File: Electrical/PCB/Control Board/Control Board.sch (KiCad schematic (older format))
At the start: 89 parts, among them J1 ED2627-ND, J10 6posheader, J11 S7038-ND, J12 ED2989-ND-USB, J13 ED1501-ND, J14 ED2989-ND-USB, J15 ED2580-ND, J16 ED2580-ND, J17 ED2744-ND, J18 ED2744-ND, J19 ED2744-ND, J2 ED2627-ND, J20 ED2744-ND, J21 ED2744-ND, J22 ED2744-ND, J23 ED2744-ND, J24 ED2744-ND, J25 ED2744-ND, J26 ED2744-ND, J3 ED2627-ND, J4 ED2627-ND, J5 ED2627-ND, J6 S9175-ND, J7 S9175-ND, J8 6posheader, J9 S7038-ND, M1 Mounting_Holes, T1 test_point, T10 test_point, T11 test_point, T12 test_point, T13 test_point, T14 test_point, T15 test_point, T16 test_point, T17 test_point, T18 test_point, T19 test_point, T2 test_point, T20 test_point, T21 test_point, T3 test_point, T4 test_point, T5 test_point, T6 test_point, T7 test_point, T8 test_point, T9 test_point, U1 LM358-N, U2 LM358-N, y1 rover_silkscreen

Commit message: Initial PCB corrections
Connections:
- wire segments 460 -> 462
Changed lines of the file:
@@
 EESchema Schematic File Version 4
-LIBS:Control Board-cache
-EELAYER 26 0
+EELAYER 30 0
 EELAYER END
 $Descr A3 16535 11693
@@
 	-1   0    0    -1
 $EndComp
-Text Label 6150 7300 0    50   ~ 0
-+BATT
 $Comp
 L Control-Board-rescue:#6THRU-HOLE-JPL_Robotics_Lib-Monolithic-Board-rescue MH1
@@
 	5950 6100 6150 6100
 Wire Wire Line
-	5900 7300 6150 7300
-Wire Wire Line
-	14200 8150 14600 8150
+	5900 7300 6100 7300
+Wire Wire Line
+	14200 8150 14500 8150
 Wire Wire Line
 	6150 6050 6150 6100
@@
 	1    0    0    -1
 $EndComp
+Connection ~ 14500 8150
+Wire Wire Line
+	14500 8150 14600 8150
+Connection ~ 5650 6100
+Connection ~ 6100 7300
+Text Label 6100 7300 0    50   ~ 0
++BATT
+Wire Wire Line
+	6100 7300 6400 7300
 $EndSCHEMATC

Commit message: Final Rev F
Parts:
- added J28: ED2580-ND, JPL Robotics:ED2580-ND, symbol Control-Board-rescue:ED2580-ND-JPL_Robotics_Lib-Monolithic-Board-rescue
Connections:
- wire segments 462 -> 465
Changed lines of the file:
@@
 Text Label 6100 7300 0    50   ~ 0
 +BATT
+$Comp
+L Control-Board-rescue:ED2580-ND-JPL_Robotics_Lib-Monolithic-Board-rescue J28
+U 1 1 5EF81C85
+P 6600 6950
+F 0 "J28" V 6500 7100 30  0000 R CNN
+F 1 "ED2580-ND" V 6450 7150 30  0001 R CNN
+F 2 "JPL Robotics:ED2580-ND" H 6600 7150 30  0001 C CNN
+F 3 "" H 6600 7150 30  0001 C CNN
+	1    6600 6950
+	-1   0    0    -1
+$EndComp
 Wire Wire Line
-	6100 7300 6400 7300
+	6450 6900 6450 7300
+Wire Wire Line
+	6100 7300 6450 7300
+Wire Wire Line
+	6250 6100 6450 6100
+Wire Wire Line
+	6450 6100 6450 6850
+Connection ~ 6250 6100
 $EndSCHEMATC

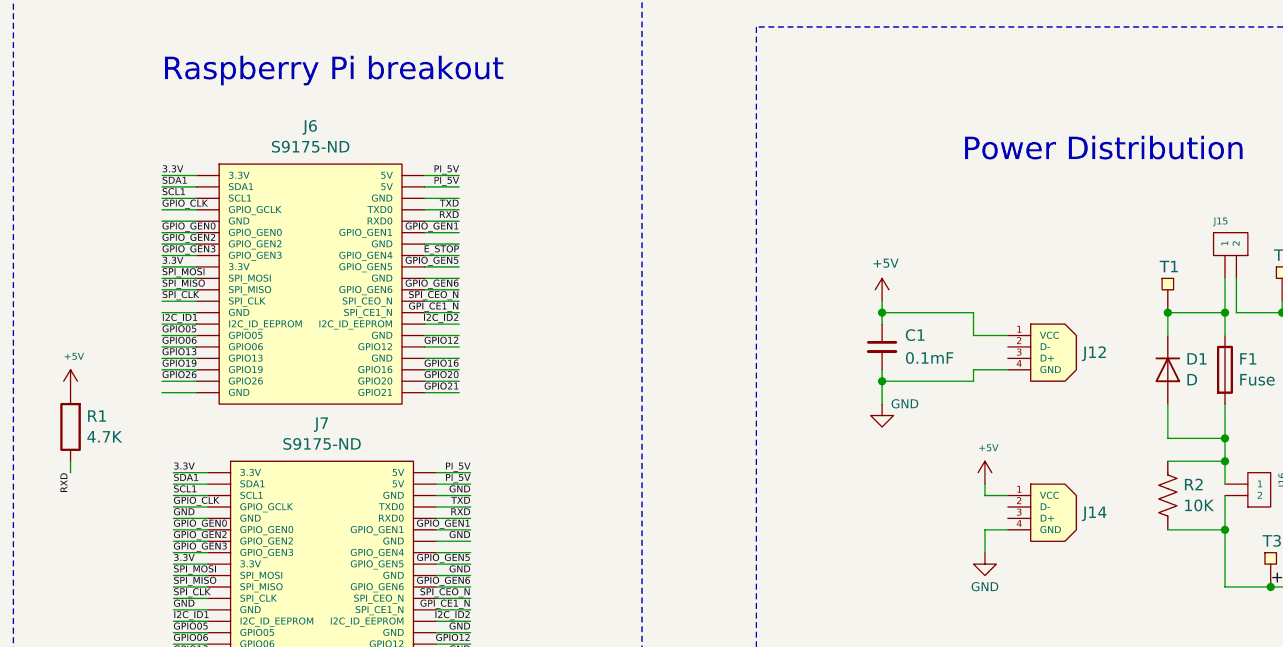
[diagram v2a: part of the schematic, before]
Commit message: Voltage and ground changes to J6 and J7, eliminate J12 and C1
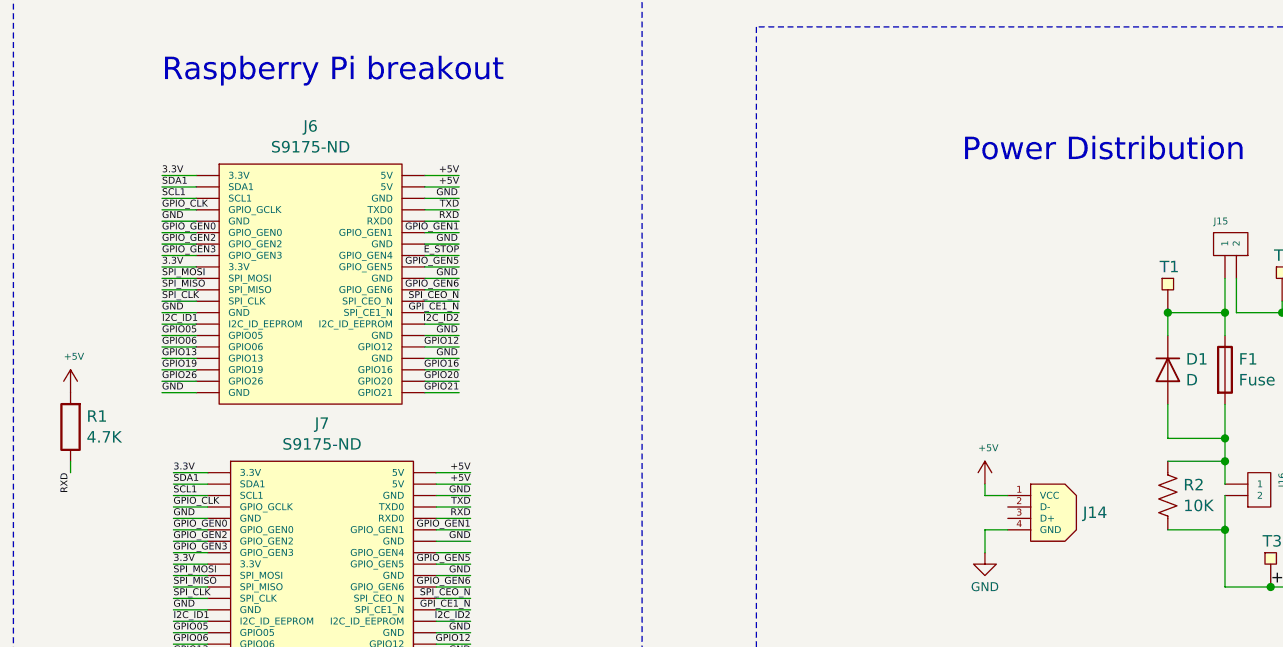
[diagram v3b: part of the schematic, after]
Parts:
- removed C1: 0.1mF, Resistor_THT:R_Axial_DIN0207_L6.3mm_D2.5mm_P7.62mm_Horizontal, symbol Device:C_Small
- removed J12: ED2989-ND-USB, JPL Robotics:ED2989-ND USB Conn, symbol Control-Board-rescue:ED2989-ND-USB-JPL_Robotics_Lib-Monolithic-Board-rescue
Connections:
- net labels removed: PI_5V
- wire segments 465 -> 455
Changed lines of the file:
@@
 GPIO26
 Text Label 2550 5500 2    30   ~ 0
-PI_5V
++5V
 Text Label 2550 5550 2    30   ~ 0
-PI_5V
++5V
 Text Label 2550 5650 2    30   ~ 0
 TXD
@@
 GND
 Text Label 2600 6800 2    30   ~ 0
-PI_5V
++5V
 Text Label 2600 6850 2    30   ~ 0
-PI_5V
++5V
 Text Label 2600 6900 2    30   ~ 0
 GND
@@
 	14000 6300 14000 6600
 $Comp
-L Device:C_Small C1
-U 1 1 5C660555
-P 4400 6250
-F 0 "C1" H 4500 6300 50  0000 L CNN
-F 1 "0.1mF" H 4500 6200 50  0000 L CNN
-F 2 "Resistor_THT:R_Axial_DIN0207_L6.3mm_D2.5mm_P7.62mm_Horizontal" H 4400 6250 50  0001 C CNN
-F 3 "~" H 4400 6250 50  0001 C CNN
-	1    4400 6250
-	1    0    0    -1
-$EndComp
-$Comp
 L Device:C_Small C2
 U 1 1 5C799779
@@
 Wire Wire Line
 	4550 1750 4750 1750
-$Comp
-L Control-Board-rescue:ED2989-ND-USB-JPL_Robotics_Lib-Monolithic-Board-rescue J12
-U 1 1 5C5F8A30
-P 4800 6350
-F 0 "J12" H 5278 6425 50  0000 L CNN
-F 1 "ED2989-ND-USB" H 5277 6380 50  0001 L CNN
-F 2 "JPL Robotics:ED2989-ND USB Conn" H 4800 6350 50  0001 C CNN
-F 3 "" H 4800 6350 50  0001 C CNN
-	1    4800 6350
-	1    0    0    -1
-$EndComp
 $Comp
 L power:GND #PWR03
@@
 RoboClaw Pin Header
 $Comp
-L power:+5V #PWR018
-U 1 1 5C776606
-P 4400 6050
-F 0 "#PWR018" H 4400 5900 50  0001 C CNN
-F 1 "+5V" H 4415 6215 39  0000 C CNN
-F 2 "" H 4400 6050 50  0001 C CNN
-F 3 "" H 4400 6050 50  0001 C CNN
-	1    4400 6050
-	1    0    0    -1
-$EndComp
-Wire Wire Line
-	4400 6050 4400 6100
-$Comp
-L power:GND #PWR019
-U 1 1 5C859B9F
-P 4400 6500
-F 0 "#PWR019" H 4400 6250 50  0001 C CNN
-F 1 "GND" H 4500 6500 39  0000 C CNN
-F 2 "" H 4400 6500 50  0001 C CNN
-F 3 "" H 4400 6500 50  0001 C CNN
-	1    4400 6500
-	1    0    0    -1
-$EndComp
-Wire Wire Line
-	4400 6500 4400 6400
-Wire Wire Line
-	4400 6100 4800 6100
-Wire Wire Line
-	4800 6100 4800 6200
-Wire Wire Line
-	4800 6200 4950 6200
-Connection ~ 4400 6100
-Wire Wire Line
-	4400 6100 4400 6150
-Wire Wire Line
-	4950 6350 4800 6350
-Wire Wire Line
-	4800 6350 4800 6400
-Wire Wire Line
-	4800 6400 4400 6400
-Connection ~ 4400 6400
-Wire Wire Line
-	4400 6400 4400 6350
-$Comp
 L power:GND #PWR032
 U 1 1 5C9B3A9C
@@
 	6450 6100 6450 6850
 Connection ~ 6250 6100
+Text Label 2450 5600 0    30   ~ 0
+GND
+Text Label 2450 5800 0    30   ~ 0
+GND
+Text Label 2450 5950 0    30   ~ 0
+GND
+Text Label 2450 6200 0    30   ~ 0
+GND
+Text Label 2450 6300 0    30   ~ 0
+GND
+Text Label 1250 6450 0    30   ~ 0
+GND
+Text Label 1250 6100 0    30   ~ 0
+GND
+Text Label 1250 5700 0    30   ~ 0
+GND
 $EndSCHEMATC

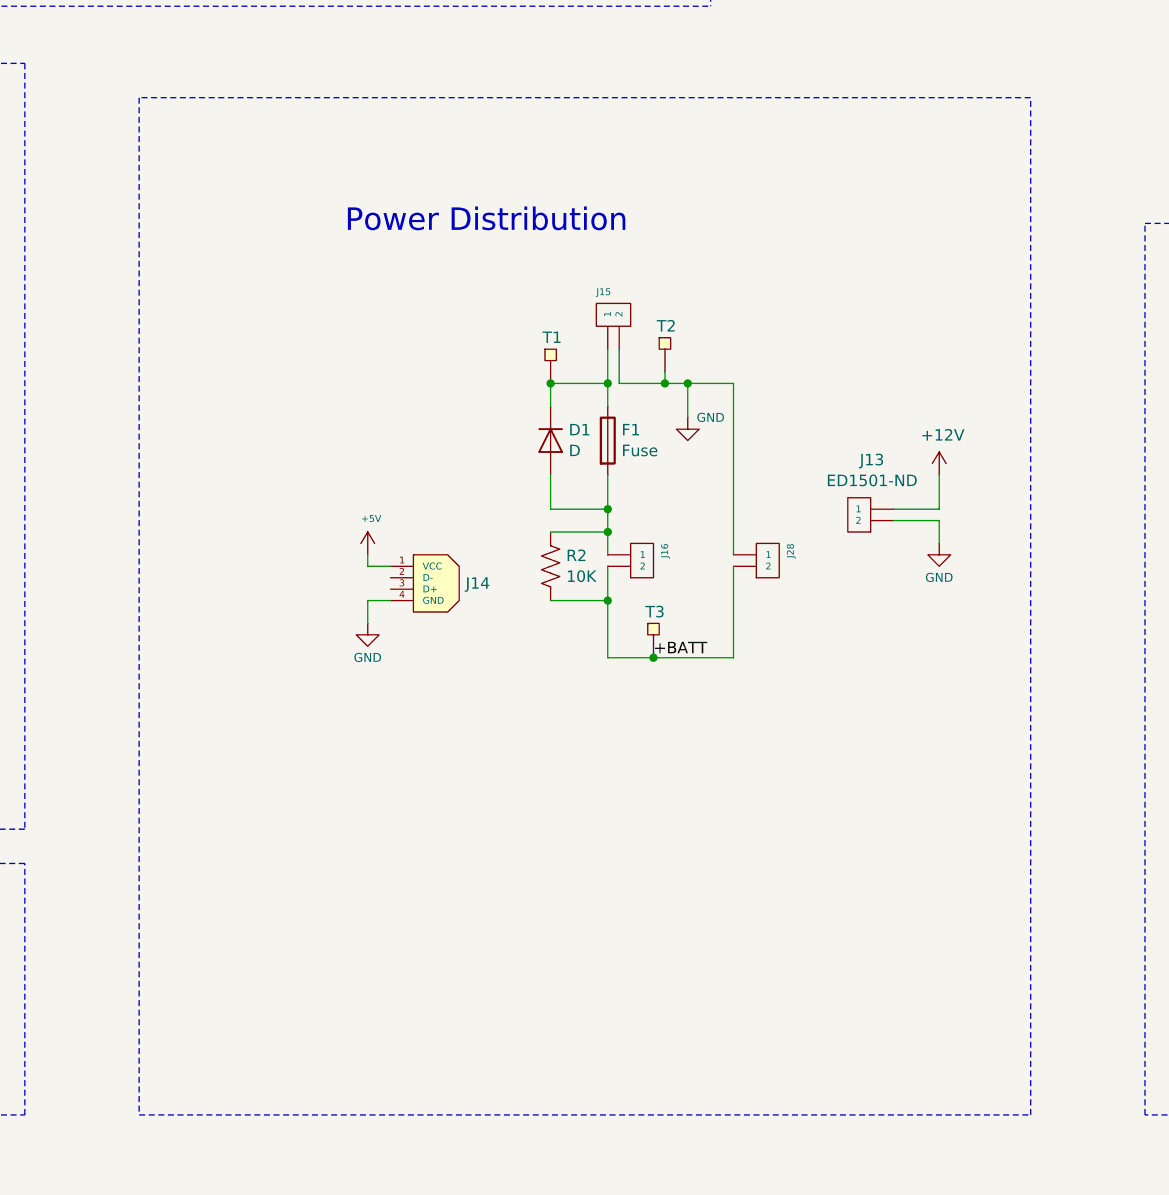
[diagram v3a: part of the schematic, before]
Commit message: Updated battery, switch, and meter connections
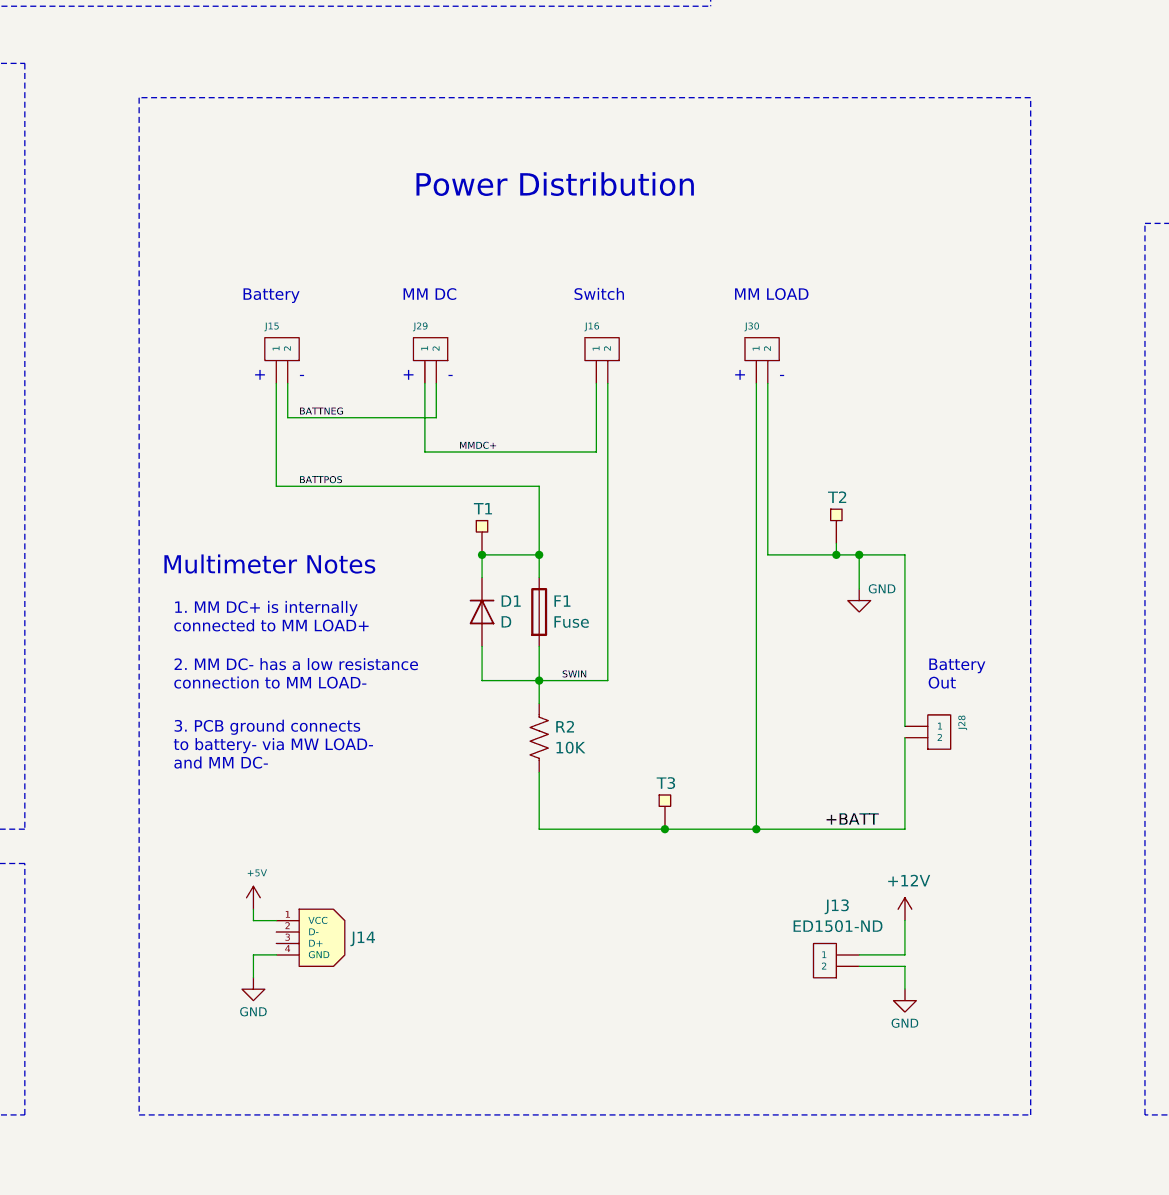
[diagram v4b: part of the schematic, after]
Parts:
- added J29, J30: ED2580-ND, JPL Robotics:ED2580-ND, symbol Control-Board-rescue:ED2580-ND-JPL_Robotics_Lib-Monolithic-Board-rescue
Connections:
- net labels added: BATTNEG, BATTPOS, MMDC+, SWIN
- wire segments 455 -> 463
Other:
- note added: "+"
- note added: "-"
- note added: "1. MM DC+ is internally \nconnected to MM LOAD+"
- note added: "2. MM DC- has a low resistance \nconnection to MM LOAD-"
- note added: "3. PCB ground connects\nto battery- via MW LOAD-\nand MM DC-"
- note added: "Battery"
- note added: "Battery\nOut"
- note added: "MM DC"
- note added: "MM LOAD"
- note added: "Multimeter Notes"
- note added: "Switch"
- moved on the sheet: D1, F1, J13, J14, J15, J16, J28, R2, T1, T2, T3

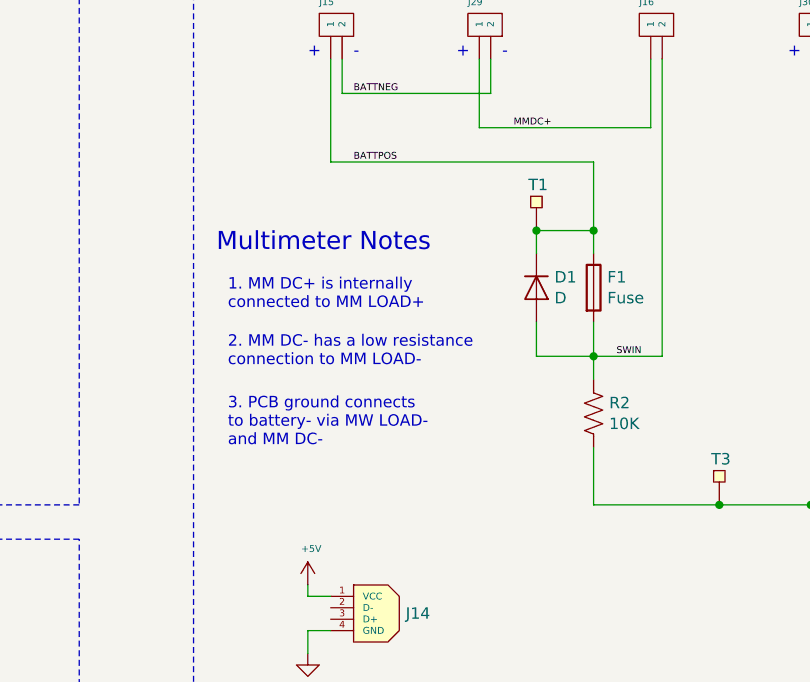
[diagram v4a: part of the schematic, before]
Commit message: Added digital voltage and current monitoring
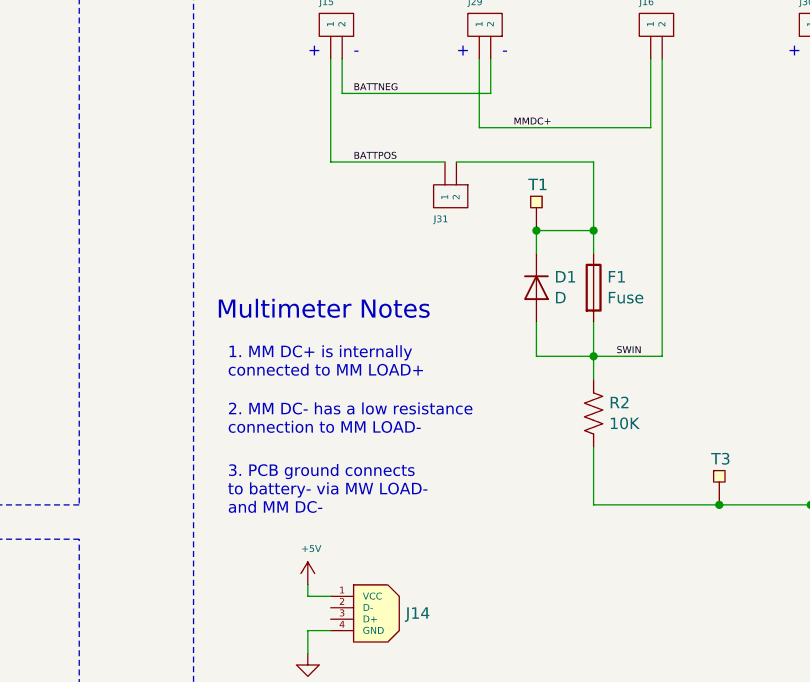
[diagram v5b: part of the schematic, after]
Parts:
- added J31: ED2580-ND, JPL Robotics:ED2580-ND, symbol Control-Board-rescue:ED2580-ND-JPL_Robotics_Lib-Monolithic-Board-rescue
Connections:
- wire segments 463 -> 464
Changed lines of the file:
@@
 	4450 6100 4450 6550
-Wire Wire Line
-	4450 6550 5600 6550
 Wire Wire Line
 	4500 6100 4500 6250
@@
 	0    -1   1    0
 $EndComp
-Text Notes 3950 6950 0    79   ~ 0
+Text Notes 3950 7250 0    79   ~ 0
 Multimeter Notes
-Text Notes 4000 7200 0    50   ~ 0
+Text Notes 4000 7500 0    50   ~ 0
 1. MM DC+ is internally \nconnected to MM LOAD+
-Text Notes 4000 7450 0    50   ~ 0
+Text Notes 4000 7750 0    50   ~ 0
 2. MM DC- has a low resistance \nconnection to MM LOAD-
 Connection ~ 6150 8050
@@
 Text Notes 6650 6100 0    50   ~ 0
 -
-Text Notes 4000 7800 0    50   ~ 0
+Text Notes 4000 8100 0    50   ~ 0
 3. PCB ground connects\nto battery- via MW LOAD-\nand MM DC-
 Text Label 4550 6550 0    30   ~ 0
@@
 Text Label 5700 7400 0    30   ~ 0
 SWIN
+$Comp
+L Control-Board-rescue:ED2580-ND-JPL_Robotics_Lib-Monolithic-Board-rescue J31
+U 1 1 5F1E1CAE
+P 5050 6700
+F 0 "J31" V 4950 6850 30  0000 R CNN
+F 1 "ED2580-ND" V 4900 6900 30  0001 R CNN
+F 2 "JPL Robotics:ED2580-ND" H 5050 6900 30  0001 C CNN
+F 3 "" H 5050 6900 30  0001 C CNN
+	1    5050 6700
+	0    -1   -1   0
+$EndComp
+Wire Wire Line
+	4450 6550 4950 6550
+Wire Wire Line
+	5000 6550 5600 6550
 $EndSCHEMATC

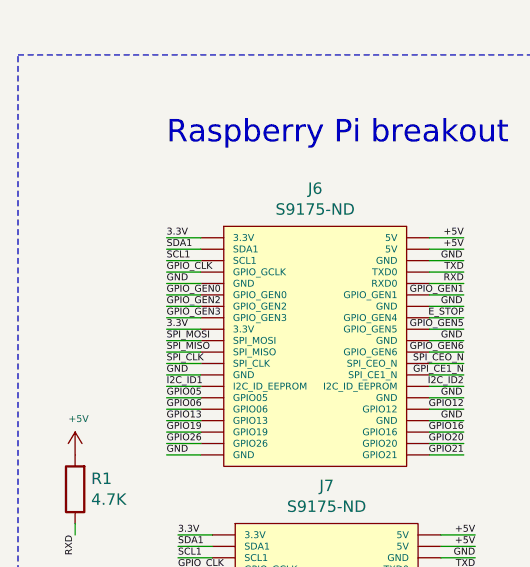
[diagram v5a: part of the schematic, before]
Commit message: moved test points, added 3.3V decoupling capacitor
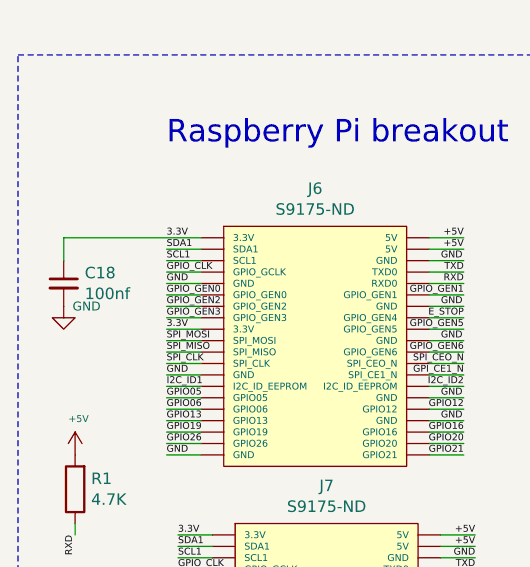
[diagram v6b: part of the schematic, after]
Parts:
- added C18: 100nf, Resistor_THT:R_Axial_DIN0207_L6.3mm_D2.5mm_P7.62mm_Horizontal, symbol Device:C_Small
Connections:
- wire segments 464 -> 465
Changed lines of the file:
@@
 RXD
-Wire Wire Line
-	1400 5500 1250 5500
 Wire Wire Line
 	1400 5550 1250 5550
@@
 Wire Wire Line
 	5000 6550 5600 6550
+$Comp
+L Device:C_Small C18
+U 1 1 5F265055
+P 800 5700
+F 0 "C18" H 892 5746 50  0000 L CNN
+F 1 "100nf" H 892 5655 50  0000 L CNN
+F 2 "Resistor_THT:R_Axial_DIN0207_L6.3mm_D2.5mm_P7.62mm_Horizontal" H 800 5700 50  0001 C CNN
+F 3 "~" H 800 5700 50  0001 C CNN
+	1    800  5700
+	1    0    0    -1
+$EndComp
+$Comp
+L power:GND #PWR0103
+U 1 1 5F2A8883
+P 800 5800
+F 0 "#PWR0103" H 800 5550 50  0001 C CNN
+F 1 "GND" H 900 5800 39  0000 C CNN
+F 2 "" H 800 5800 50  0001 C CNN
+F 3 "" H 800 5800 50  0001 C CNN
+	1    800  5800
+	1    0    0    -1
+$EndComp
+Wire Wire Line
+	800  5500 1400 5500
+Wire Wire Line
+	800  5500 800  5600
 $EndSCHEMATC
